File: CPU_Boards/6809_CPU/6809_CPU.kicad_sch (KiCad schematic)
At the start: 68 parts, among them J16 ., J17 ., J18 ., J19 ., J20 Conn_01x12, J21 Conn_01x12, J22 Conn_01x12, J23 Conn_01x12, J24 GAL_20x10, J25 GAL_20x10, J26 Conn_01x12, J27 ., J28 ., J29 ., J32 ., J33 ., J34 JTAG, J35 Conn_01x12, J36 Spare, J37 Outside, J38 Conn_01x12, J39 GAL_20x10, J40 Conn_01x12, J41 Conn_02x02_Odd_Even, J42 Conn_02x02_Odd_Even, J5 Conn_01x09, J6 Conn_01x08, J7 Conn_01x08, J8 Conn_01x09, J9 ., U1 XC9572VQ44, U22 MC6809E, U23 MC6809

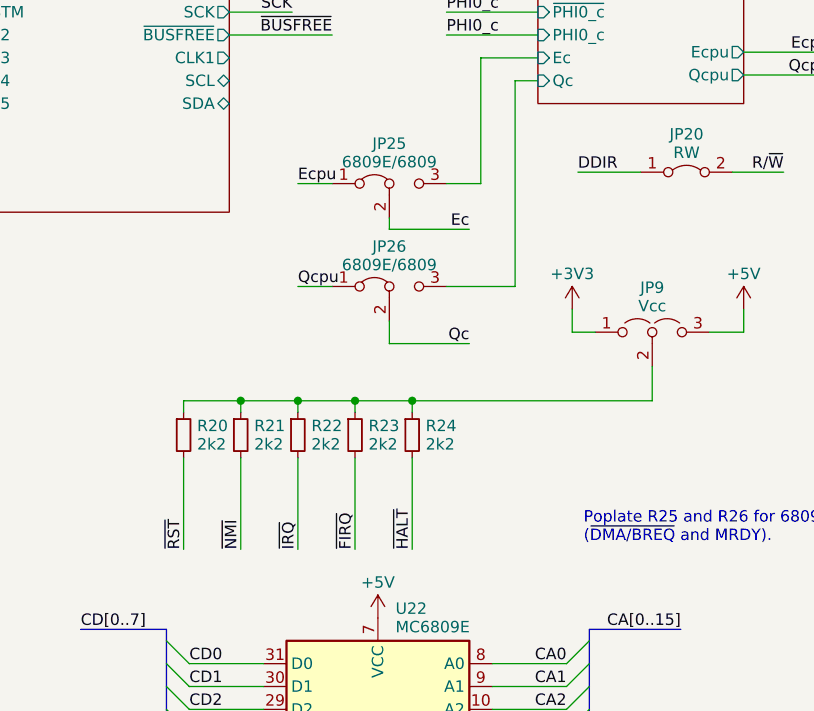
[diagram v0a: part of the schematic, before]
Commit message: first boards manufactured
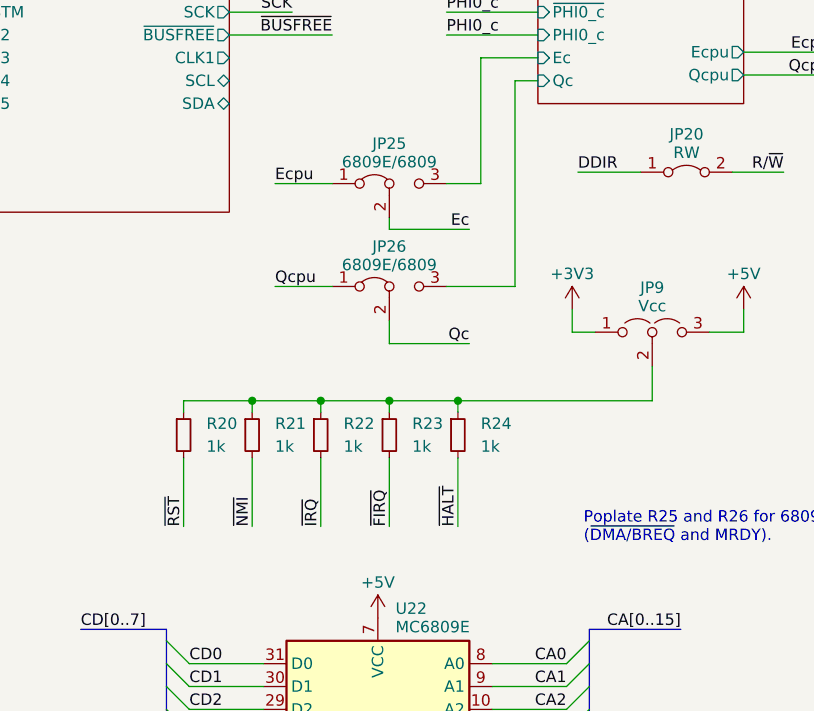
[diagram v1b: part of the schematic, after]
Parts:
- J16, J17, J18, J19, J20, J21, J22, J23, J24, J25, J26, J27, J28, J29, J32, J33, J35, J36, J38, J39, J40, J41, J42, J5, J6, J7, J8, J9, JP10, JP11, JP12, JP13, JP14, JP15, JP20, JP21, JP22, JP23, JP24, JP25, JP26, JP27, JP9: now left out of the parts list
- R20, R21, R22, R23, R24: value 2k2 -> 1k
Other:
- moved on the sheet: R21, R22, R23, R24
